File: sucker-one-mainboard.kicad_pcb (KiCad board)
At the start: 4 copper layers, 68 x 67.3 mm, 126 parts, among them J1 JST NC Valve, J10 BM10B-SRSS-TB(LF)(SN), J11 UART/SWD DNP, J12 TYPE-C-31-M-12, J2 JST NO Valve, J3 6P4C, J4 JST 3 Way Valve, J5 Jack-DC, J6 Phoenix Contact 1733570, J7 QWIIC I2C, J8 SPI, J9 BM04B-SRSS-TBT(LF)(SN), Q1 BSS138, Q2 BSS138, Q3 BSS138, Q4 STN4NF20L, Q5 BSS138, SW1 BOOTSEL, U1 LD1117S33TR, U2 TPS62143RGTT, U3 W25Q128JVPIQ TR, U4 RP2040, Y1 ABMM2-12.000MHZ-E2-T

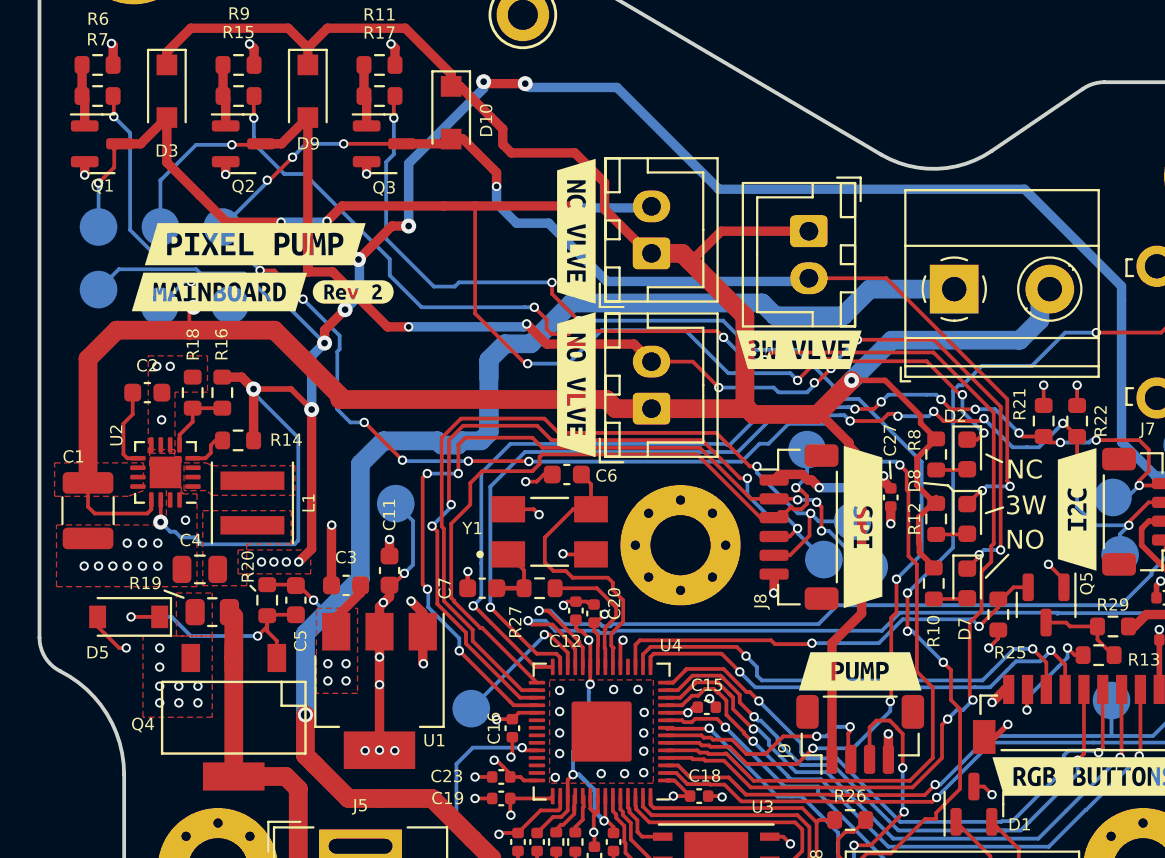
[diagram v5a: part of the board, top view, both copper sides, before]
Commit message: Changed Buck Converter
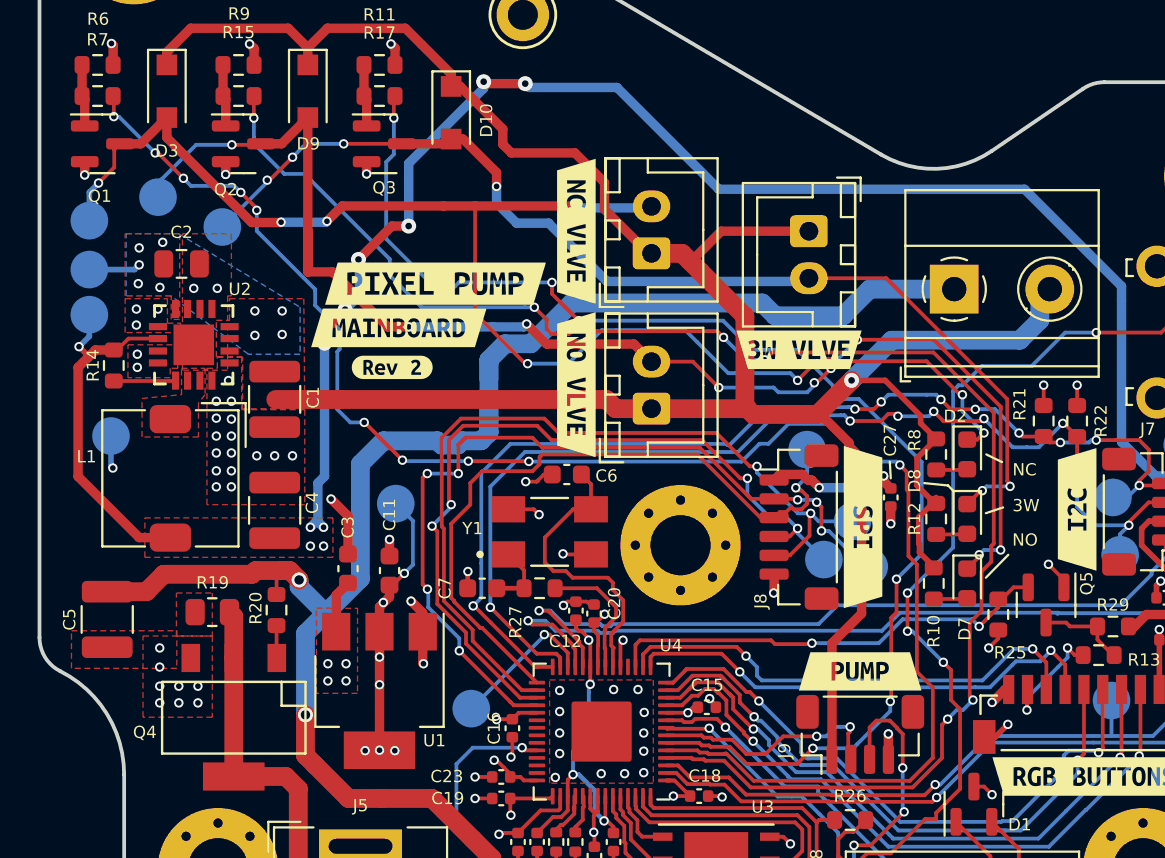
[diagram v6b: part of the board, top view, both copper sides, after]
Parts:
- removed D5: DDZ9697-7 10v 500mW DNP, Diode_SMD:D_SOD-123
- removed R16: 19k, Resistor_SMD:R_0603_1608Metric
- removed R18: 99.7k, Resistor_SMD:R_0603_1608Metric
- C2: value 3.3n 25V -> 1u; footprint Capacitor_SMD:C_0603_1608Metric -> Capacitor_SMD:C_0805_2012Metric
- C4: value 22u 10v -> 22u 10V; footprint Capacitor_SMD:C_0805_2012Metric -> Capacitor_SMD:C_1210_3225Metric
- C5: value 10u 25v DNP -> 10u 25v; footprint Capacitor_SMD:C_0603_1608Metric -> Capacitor_SMD:C_1210_3225Metric
- L1: value 2.2uH 3.1A XFL4020-222MEB -> L; footprint Inductor_SMD:L_Coilcraft_XxL4020 -> Inductor_SMD:L_TDK_SLF7032
- R14: value 100k -> 1M
- U2: value TPS62143RGTT -> TPS62112RSAR; footprint Package_DFN_QFN:VQFN-16-1EP_3x3mm_P0.5mm_EP1.68x1.68mm_ThermalVias -> TPS62112RSAR:QFN65P400X400X100-17N
- moved C1 11.6 mm to (78.5, 119.5)
- moved C5 10.1 mm to (69.6, 131.2)
- moved kibuzzard-61080AF0 9.81 mm to (87.0, 113.3)
- moved kibuzzard-61080B06 9.72 mm to (85.1, 115.7)
- moved R14 7.71 mm to (70.0, 117.7), turned to -90 degrees
- moved TP10 7.71 mm to (68.7, 112.6)
- moved TP13 7.37 mm to (69.8, 121.5)
- moved C2 7.08 mm to (73.5, 112.3)
- moved U2 6.95 mm to (74.2, 116.6)
- moved C4 5.07 mm to (78.5, 125.4), turned to 90 degrees
- moved L1 4.55 mm to (73.0, 123.7)
- moved kibuzzard-61080B37 4.51 mm to (84.8, 117.8)
- moved TP7 1.59 mm to (72.3, 108.8)
- moved TP16 1.42 mm to (68.7, 115.0)
- moved C3 0.89 mm to (82.4, 128.5), turned to 90 degrees
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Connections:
- C2 pad 1: Net-(C2-Pad1) -> +12V
- C5 pad 2: Net-(C5-Pad2) -> GND
- Q4 pad 1: Net-(C5-Pad2) -> Net-(Q4-Pad1)
- R20 pad 2: Net-(C5-Pad2) -> Net-(Q4-Pad1)
- U2 pad 1: Net-(L1-Pad1) -> GND
- U2 pad 10: +12V -> +5V
- U2 pad 11: +12V -> GND
- U2 pad 12: +12V -> GND
- U2 pad 13: +12V -> Net-(R14-Pad2)
- U2 pad 14: +5V -> Net-(L1-Pad1)
- U2 pad 15: GND -> Net-(L1-Pad1)
- U2 pad 2: Net-(L1-Pad1) -> +12V
- U2 pad 3: Net-(L1-Pad1) -> +12V
- U2 pad 4: Net-(R14-Pad2) -> +12V
- U2 pad 5: FB -> GND
- U2 pad 8: GND -> +12V
- U2 pad 9: Net-(C2-Pad1) -> GND
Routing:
- net +12V: track 162.0 -> 137.2 mm, vias 2 -> 10
- net +5V: track 141.4 -> 118.4 mm, vias 18 -> 16
- net Net-(C5-Pad2): track 14.0 -> 0.00 mm, vias 2 -> 0
- net Net-(C5-Pad1): track 94.5 -> 105.2 mm
- net Net-(C2-Pad1): track 4.34 -> 0.00 mm
- net FB: track 3.82 -> 0.00 mm
- net GND: track 61.5 -> 58.1 mm, vias 81 -> 90
- net Net-(D7-Pad1): track 74.5 -> 72.0 mm
- net Net-(Q4-Pad1): track 0.00 -> 1.73 mm
- net NC_VALVE: track 89.4 -> 87.7 mm, vias 8 -> 10
- net Net-(R14-Pad2): track 2.21 -> 3.29 mm
- net Net-(D2-Pad1): track 77.3 -> 76.4 mm
- added copper zone on B.Cu, net +12V
